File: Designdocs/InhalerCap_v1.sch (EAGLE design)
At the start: 11 parts

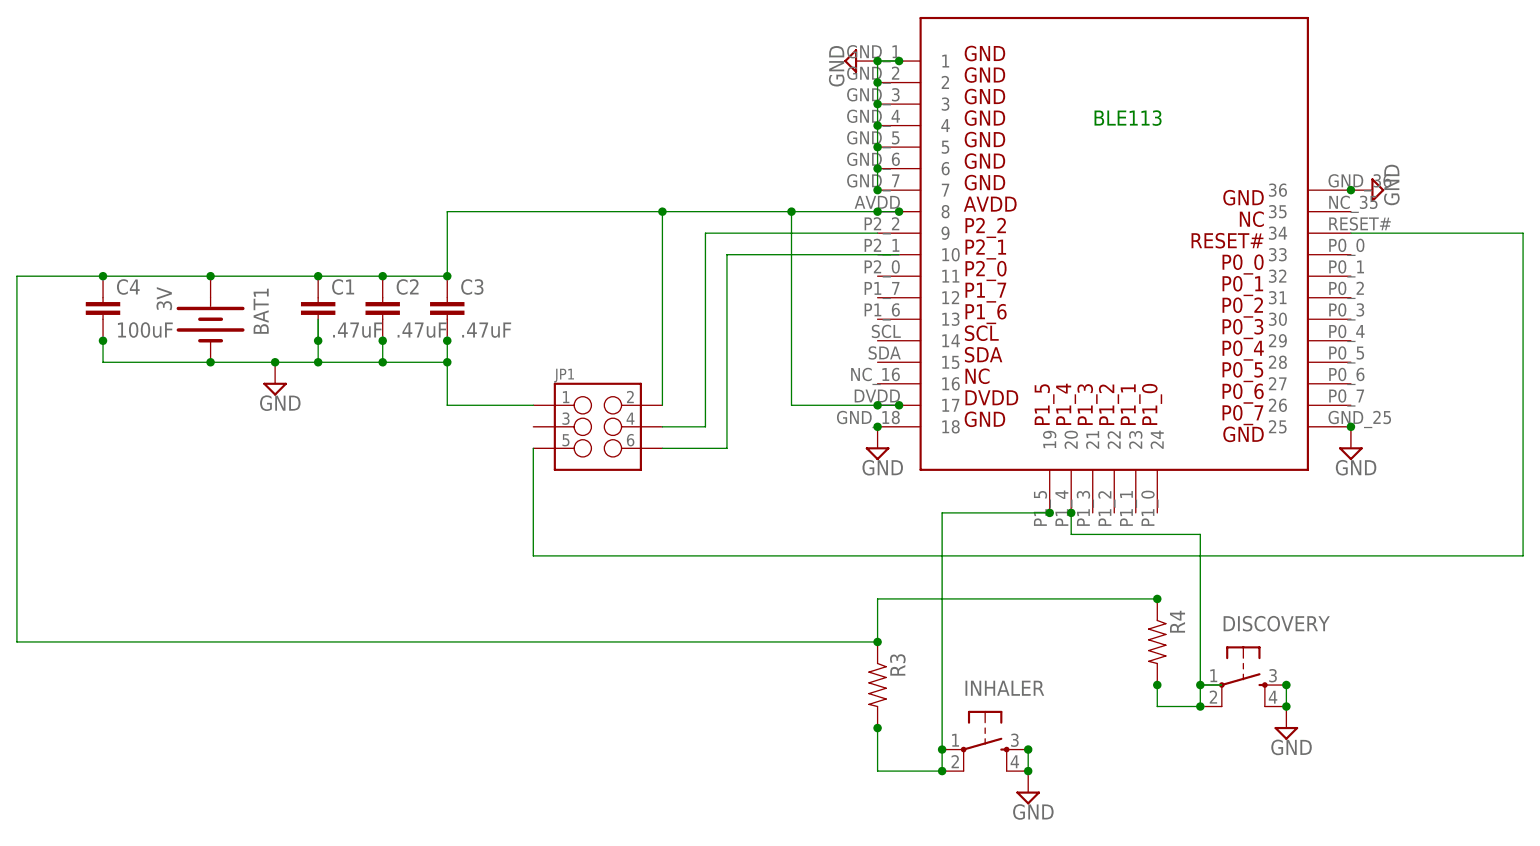
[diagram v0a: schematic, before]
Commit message: Design for simplified inhaler cap
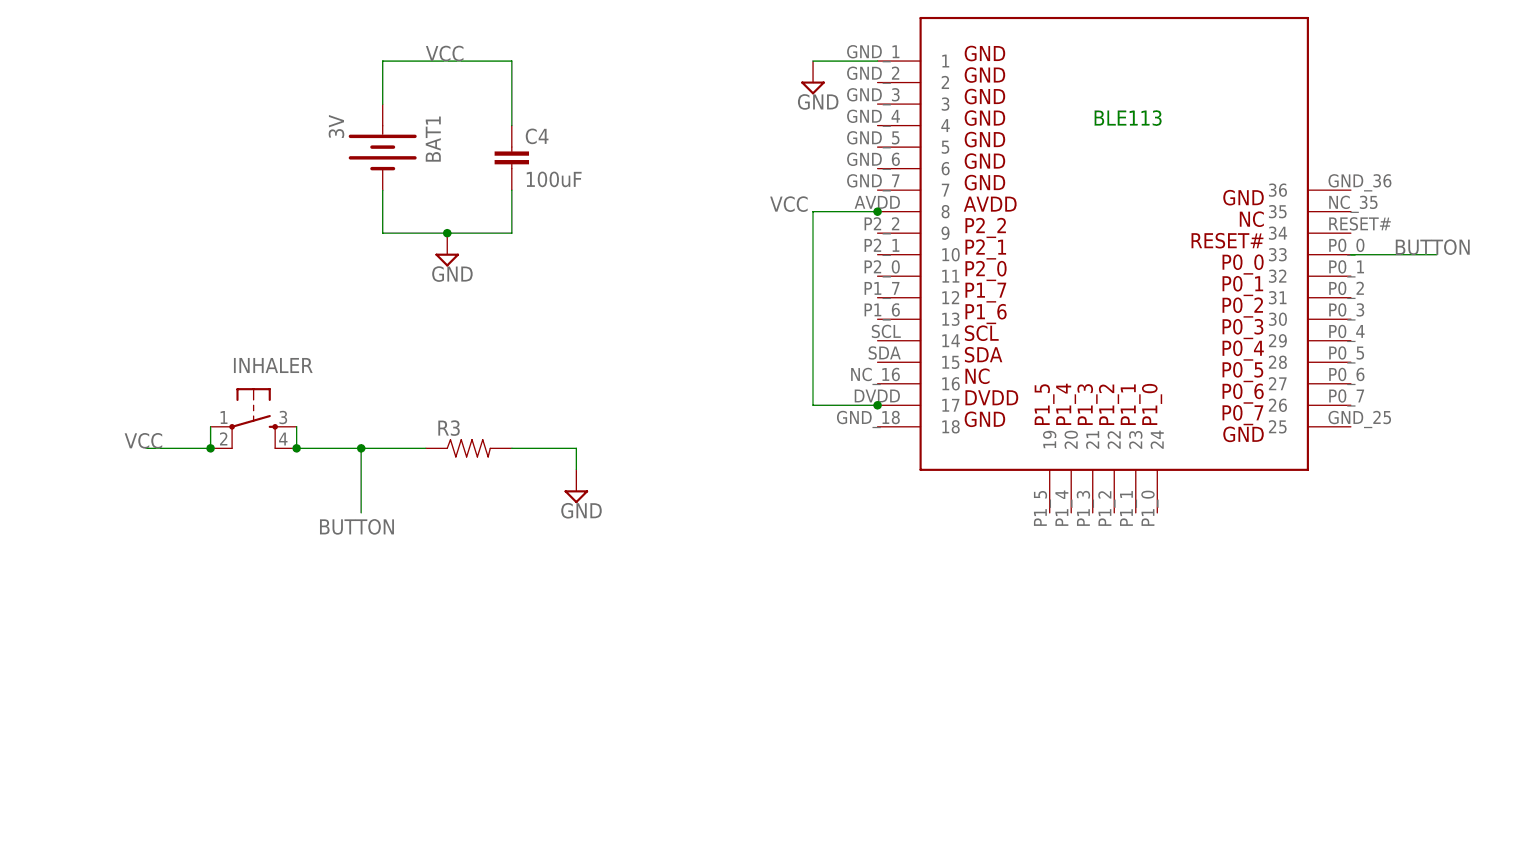
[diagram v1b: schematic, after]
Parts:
- removed C1, C2, C3: .47uF, SparkFun-Capacitors:CAP0603-CAP
- removed DISCOVERY: (no value), SparkFun-Electromechanical:TAC_SWITCHSMD
- removed JP1: (no value), SparkFun-Connectors:M03X22X3_SILK_SM
- removed R4: (no value), SparkFun-Passives:RESISTOR0603-RES
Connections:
- removed net N$10: DISCOVERY.2, R4.2, U$1.20
- removed net N$2: BAT1.+, C1.1, C2.1, C3.1, C4.1, JP1.2, R3.1, R4.1, U$1.17, U$1.8
- removed net N$4: JP1.4, U$1.9
- removed net N$5: JP1.6
- removed net N$6: JP1.5, U$1.34
- removed net N$8: INHALER.1, INHALER.2, R3.2, U$1.19
- new net BUTTON: INHALER.3, INHALER.4, R3.1, U$1.33
- new net VCC: BAT1.+, C4.1, INHALER.1, INHALER.2, U$1.17, U$1.8
- net GND: now also R3.2; no longer C1.2, C2.2, C3.2, DISCOVERY.3, DISCOVERY.4, INHALER.3, INHALER.4, JP1.1, U$1.18, U$1.2, U$1.25, U$1.3, U$1.36, U$1.4, U$1.5, U$1.6, U$1.7
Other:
- moved on the sheet: BAT1, C4, INHALER, R3

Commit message: Updated documentation
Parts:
- removed BAT1: 3V, SparkFun-Electromechanical:BATTERY20SMD
- added BAT2: 20mm coincell, SparkFun-Electromechanical:BATTERY20MM_4LEGS
- added BUTTON, GND, P2_1, P2_2, RESET, VCC: TPTP20SQ, testpad:TPTP20SQ
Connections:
- new net 1: INHALER.4, R3.1
- new net P2_1: P2_1.TP, U$1.10
- new net P2_2: P2_2.TP, U$1.9
- new net RESET: RESET.TP, U$1.34
- net BUTTON: now also BUTTON.TP; no longer INHALER.4, R3.1
- net GND: now also BAT2.-, GND.TP; no longer BAT1.-
- net VCC: now also BAT2.+, VCC.TP; no longer BAT1.+, INHALER.2
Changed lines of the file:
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@@
 <part name="U$1" library="BLE113-A" deviceset="BLE113-A" device=""/>
 <part name="C4" library="SparkFun-Capacitors" deviceset="CAP" device="1206" value="100uF"/>
-<part name="BAT1" library="SparkFun-Electromechanical" deviceset="BATTERY" device="20SMD" value="3V"/>
 <part name="R3" library="SparkFun-Passives" deviceset="RESISTOR" device="0603-RES"/>
 <part name="INHALER" library="SparkFun-Electromechanical" deviceset="TAC_SWITCH" device="SMD"/>
@@
 <part name="SUPPLY6" library="supply2" deviceset="GND" device=""/>
 <part name="SUPPLY1" library="supply2" deviceset="GND" device=""/>
+<part name="BAT2" library="SparkFun-Electromechanical" deviceset="BATTERY" device="20MM_4LEGS" value="20mm coincell"/>
+<part name="VCC" library="testpad" deviceset="TP" device="TP20SQ"/>
+<part name="GND" library="testpad" deviceset="TP" device="TP20SQ"/>
+<part name="P2_2" library="testpad" deviceset="TP" device="TP20SQ"/>
+<part name="P2_1" library="testpad" deviceset="TP" device="TP20SQ"/>
+<part name="RESET" library="testpad" deviceset="TP" device="TP20SQ"/>
+<part name="BUTTON" library="testpad" deviceset="TP" device="TP20SQ"/>
 </parts>
 <sheets>
@@
 <instance part="U$1" gate="G$1" x="88.9" y="78.74"/>
 <instance part="C4" gate="G$1" x="40.64" y="66.04"/>
-<instance part="BAT1" gate="G$1" x="25.4" y="68.58" rot="R270"/>
 <instance part="R3" gate="G$1" x="35.56" y="33.02"/>
 <instance part="INHALER" gate="S" x="10.16" y="35.56"/>
@@
 <instance part="SUPPLY6" gate="GND" x="76.2" y="76.2"/>
 <instance part="SUPPLY1" gate="GND" x="33.02" y="55.88"/>
+<instance part="BAT2" gate="G$1" x="25.4" y="68.58" rot="R270"/>
+<instance part="VCC" gate="G$1" x="66.04" y="12.7"/>
+<instance part="GND" gate="G$1" x="73.66" y="12.7"/>
+<instance part="P2_2" gate="G$1" x="81.28" y="12.7"/>
+<instance part="P2_1" gate="G$1" x="88.9" y="12.7"/>
+<instance part="RESET" gate="G$1" x="96.52" y="12.7"/>
+<instance part="BUTTON" gate="G$1" x="106.68" y="12.7"/>
 </instances>
 <busses>
@@
 </segment>
 <segment>
-<pinref part="BAT1" gate="G$1" pin="-"/>
 <wire x1="25.4" y1="63.5" x2="25.4" y2="58.42" width="0.1524" layer="91"/>
 <pinref part="C4" gate="G$1" pin="2"/>
@@
 <wire x1="33.02" y1="58.42" x2="25.4" y2="58.42" width="0.1524" layer="91"/>
 <junction x="33.02" y="58.42"/>
+<pinref part="BAT2" gate="G$1" pin="-"/>
 </segment>
 <segment>
@@
 <wire x1="48.26" y1="33.02" x2="40.64" y2="33.02" width="0.1524" layer="91"/>
 </segment>
+<segment>
+<pinref part="GND" gate="G$1" pin="TP"/>
+<junction x="73.66" y="10.16"/>
+</segment>
 </net>
 <net name="VCC" class="0">
@@
 <pinref part="C4" gate="G$1" pin="1"/>
 <wire x1="40.64" y1="78.74" x2="40.64" y2="71.12" width="0.1524" layer="91"/>
-<pinref part="BAT1" gate="G$1" pin="+"/>
 <wire x1="25.4" y1="73.66" x2="25.4" y2="78.74" width="0.1524" layer="91"/>
 <wire x1="25.4" y1="78.74" x2="40.64" y2="78.74" width="0.1524" layer="91"/>
 <label x="30.48" y="78.74" size="1.778" layer="95"/>
+<pinref part="BAT2" gate="G$1" pin="+"/>
 </segment>
 <segment>
@@
 </segment>
 <segment>
-<pinref part="INHALER" gate="S" pin="2"/>
+<pinref part="VCC" gate="G$1" pin="TP"/>
+<junction x="66.04" y="10.16"/>
+</segment>
+<segment>
 <pinref part="INHALER" gate="S" pin="1"/>
-<wire x1="5.08" y1="33.02" x2="5.08" y2="35.56" width="0.1524" layer="91"/>
-<wire x1="5.08" y1="33.02" x2="-2.54" y2="33.02" width="0.1524" layer="91"/>
-<junction x="5.08" y="33.02"/>
-<label x="-5.08" y="33.02" size="1.778" layer="95"/>
+<junction x="5.08" y="35.56"/>
+<label x="0" y="35.56" size="1.778" layer="95"/>
 </segment>
 </net>
 <net name="BUTTON" class="0">
 <segment>
-<pinref part="R3" gate="G$1" pin="1"/>
-<pinref part="INHALER" gate="S" pin="4"/>
-<wire x1="30.48" y1="33.02" x2="22.86" y2="33.02" width="0.1524" layer="91"/>
-<pinref part="INHALER" gate="S" pin="3"/>
-<wire x1="22.86" y1="33.02" x2="15.24" y2="33.02" width="0.1524" layer="91"/>
-<wire x1="15.24" y1="35.56" x2="15.24" y2="33.02" width="0.1524" layer="91"/>
-<junction x="15.24" y="33.02"/>
-<wire x1="22.86" y1="33.02" x2="22.86" y2="25.4" width="0.1524" layer="91"/>
-<junction x="22.86" y="33.02"/>
-<label x="17.78" y="22.86" size="1.778" layer="95"/>
-</segment>
-<segment>
 <pinref part="U$1" gate="G$1" pin="33"/>
 <wire x1="139.7" y1="55.88" x2="149.86" y2="55.88" width="0.1524" layer="91"/>
 <label x="144.78" y="55.88" size="1.778" layer="95"/>
+<junction x="139.7" y="55.88"/>
+</segment>
+<segment>
+<pinref part="BUTTON" gate="G$1" pin="TP"/>
+<junction x="106.68" y="10.16"/>
+</segment>
+<segment>
+<pinref part="INHALER" gate="S" pin="3"/>
+<junction x="15.24" y="35.56"/>
+<label x="15.24" y="35.56" size="1.778" layer="95"/>
 </segment>
 </net>
+<net name="RESET" class="0">
+<segment>
+<pinref part="U$1" gate="G$1" pin="34"/>
+<wire x1="139.7" y1="58.42" x2="149.86" y2="58.42" width="0.1524" layer="91"/>
+<junction x="139.7" y="58.42"/>
+<label x="147.32" y="58.42" size="1.778" layer="95"/>
+</segment>
+<segment>
+<pinref part="RESET" gate="G$1" pin="TP"/>
+<junction x="96.52" y="10.16"/>
+</segment>
+</net>
+<net name="P2_1" class="0">
+<segment>
+<wire x1="86.36" y1="55.88" x2="83.82" y2="55.88" width="0.1524" layer="91"/>
+<pinref part="U$1" gate="G$1" pin="10"/>
+<junction x="83.82" y="55.88"/>
+<wire x1="83.82" y1="55.88" x2="81.28" y2="55.88" width="0.1524" layer="91"/>
+</segment>
+<segment>
+<pinref part="P2_1" gate="G$1" pin="TP"/>
+<junction x="88.9" y="10.16"/>
+</segment>
+</net>
+<net name="P2_2" class="0">
+<segment>
+<pinref part="U$1" gate="G$1" pin="9"/>
+<wire x1="83.82" y1="58.42" x2="81.28" y2="58.42" width="0.1524" layer="91"/>
+<junction x="83.82" y="58.42"/>
+</segment>
+<segment>
+<pinref part="P2_2" gate="G$1" pin="TP"/>
+<junction x="81.28" y="10.16"/>
+</segment>
+</net>
+<net name="1" class="0">
+<segment>
+<pinref part="R3" gate="G$1" pin="1"/>
+<pinref part="INHALER" gate="S" pin="4"/>
+<wire x1="30.48" y1="33.02" x2="15.24" y2="33.02" width="0.1524" layer="91"/>
+</segment>
+</net>
